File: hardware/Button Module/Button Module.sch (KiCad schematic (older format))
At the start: 10 parts, among them J1 1A, J2 1A, J3 2A, J4 2A, J5 1B, J6 1B, J7 2B, J8 2B, SW1 B3F-4055, SW2 B3F-4055

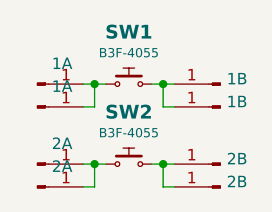
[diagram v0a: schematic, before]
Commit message: Updated instructions for RPi 4 boards
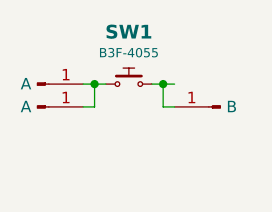
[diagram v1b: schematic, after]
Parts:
- removed J3, J4: 2A, Connector_PinHeader_2.54mm:PinHeader_1x01_P2.54mm_Vertical, symbol Connector:Conn_01x01_Male
- removed J5: 1B, Connector_PinHeader_2.54mm:PinHeader_1x01_P2.54mm_Vertical, symbol Connector:Conn_01x01_Male
- removed J7, J8: 2B, Connector_PinHeader_2.54mm:PinHeader_1x01_P2.54mm_Vertical, symbol Connector:Conn_01x01_Male
- removed SW2: B3F-4055, switches:B3F-40XX, symbol switches:MOM-SPST
- J1, J2: value 1A -> A
- J6: value 1B -> B
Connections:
- wire segments 16 -> 8
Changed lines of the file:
@@
 Comment4 ""
 $EndDescr
+Wire Wire Line
+	2750 2850 2700 2850
+Wire Wire Line
+	2800 2850 2750 2850
+Connection ~ 2750 2850
+Wire Wire Line
+	2750 2950 2750 2850
+Wire Wire Line
+	2800 2950 2750 2950
+$Comp
+L Connector:Conn_01x01_Male J6
+U 1 1 5E38EB6E
+P 3000 2950
+F 0 "J6" H 2972 2882 50  0001 R CNN
+F 1 "B" H 2950 2950 50  0000 C CNN
+F 2 "Connector_PinHeader_2.54mm:PinHeader_1x01_P2.54mm_Vertical" H 3000 2950 50  0001 C CNN
+F 3 "~" H 3000 2950 50  0001 C CNN
+	1    3000 2950
+	-1   0    0    1
+$EndComp
+$Comp
+L Connector:Conn_01x01_Male J1
+U 1 1 5E38A935
+P 2200 2850
+F 0 "J1" H 2308 3031 50  0001 C CNN
+F 1 "A" H 2150 2850 50  0000 C CNN
+F 2 "Connector_PinHeader_2.54mm:PinHeader_1x01_P2.54mm_Vertical" H 2200 2850 50  0001 C CNN
+F 3 "~" H 2200 2850 50  0001 C CNN
+	1    2200 2850
+	1    0    0    -1
+$EndComp
+Wire Wire Line
+	2400 2950 2450 2950
+$Comp
+L Connector:Conn_01x01_Male J2
+U 1 1 5E38AF59
+P 2200 2950
+F 0 "J2" H 2308 3131 50  0001 C CNN
+F 1 "A" H 2150 2950 50  0000 C CNN
+F 2 "Connector_PinHeader_2.54mm:PinHeader_1x01_P2.54mm_Vertical" H 2200 2950 50  0001 C CNN
+F 3 "~" H 2200 2950 50  0001 C CNN
+	1    2200 2950
+	1    0    0    -1
+$EndComp
+Wire Wire Line
+	2450 2850 2500 2850
+Wire Wire Line
+	2450 2950 2450 2850
+Connection ~ 2450 2850
+Wire Wire Line
+	2400 2850 2450 2850
 $Comp
 L switches:MOM-SPST SW1
@@
 	1    0    0    -1
 $EndComp
-$Comp
-L switches:MOM-SPST SW2
-U 1 1 5E389875
-P 2600 3200
-F 0 "SW2" H 2600 3427 60  0000 C CNB
-F 1 "B3F-4055" H 2600 3336 40  0000 C CNN
-F 2 "switches:B3F-40XX" H 2500 3075 40  0001 L TNN
-F 3 "" H 2525 2975 60  0001 C CNN
-F 4 "-" H 2500 3400 40  0001 L BNN "Part"
-F 5 "Switch" H 2500 3500 40  0001 L BNN "Family"
-	1    2600 3200
-	1    0    0    -1
-$EndComp
-$Comp
-L Connector:Conn_01x01_Male J1
-U 1 1 5E38A935
-P 2200 2850
-F 0 "J1" H 2308 3031 50  0001 C CNN
-F 1 "1A" H 2308 2939 50  0000 C CNN
-F 2 "Connector_PinHeader_2.54mm:PinHeader_1x01_P2.54mm_Vertical" H 2200 2850 50  0001 C CNN
-F 3 "~" H 2200 2850 50  0001 C CNN
-	1    2200 2850
-	1    0    0    -1
-$EndComp
-$Comp
-L Connector:Conn_01x01_Male J2
-U 1 1 5E38AF59
-P 2200 2950
-F 0 "J2" H 2308 3131 50  0001 C CNN
-F 1 "1A" H 2308 3039 50  0000 C CNN
-F 2 "Connector_PinHeader_2.54mm:PinHeader_1x01_P2.54mm_Vertical" H 2200 2950 50  0001 C CNN
-F 3 "~" H 2200 2950 50  0001 C CNN
-	1    2200 2950
-	1    0    0    -1
-$EndComp
-$Comp
-L Connector:Conn_01x01_Male J3
-U 1 1 5E38B268
-P 2200 3200
-F 0 "J3" H 2308 3381 50  0001 C CNN
-F 1 "2A" H 2308 3289 50  0000 C CNN
-F 2 "Connector_PinHeader_2.54mm:PinHeader_1x01_P2.54mm_Vertical" H 2200 3200 50  0001 C CNN
-F 3 "~" H 2200 3200 50  0001 C CNN
-	1    2200 3200
-	1    0    0    -1
-$EndComp
-$Comp
-L Connector:Conn_01x01_Male J4
-U 1 1 5E38B61F
-P 2200 3300
-F 0 "J4" H 2308 3481 50  0001 C CNN
-F 1 "2A" H 2308 3389 50  0000 C CNN
-F 2 "Connector_PinHeader_2.54mm:PinHeader_1x01_P2.54mm_Vertical" H 2200 3300 50  0001 C CNN
-F 3 "~" H 2200 3300 50  0001 C CNN
-	1    2200 3300
-	1    0    0    -1
-$EndComp
-Wire Wire Line
-	2400 2850 2450 2850
-Wire Wire Line
-	2400 2950 2450 2950
-Wire Wire Line
-	2450 2950 2450 2850
-Connection ~ 2450 2850
-Wire Wire Line
-	2450 2850 2500 2850
-Wire Wire Line
-	2400 3200 2450 3200
-Wire Wire Line
-	2400 3300 2450 3300
-Wire Wire Line
-	2450 3300 2450 3200
-Connection ~ 2450 3200
-Wire Wire Line
-	2450 3200 2500 3200
-$Comp
-L Connector:Conn_01x01_Male J5
-U 1 1 5E38DF3B
-P 3000 2850
-F 0 "J5" H 2972 2782 50  0001 R CNN
-F 1 "1B" H 2972 2828 50  0000 R CNN
-F 2 "Connector_PinHeader_2.54mm:PinHeader_1x01_P2.54mm_Vertical" H 3000 2850 50  0001 C CNN
-F 3 "~" H 3000 2850 50  0001 C CNN
-	1    3000 2850
-	-1   0    0    1
-$EndComp
-$Comp
-L Connector:Conn_01x01_Male J6
-U 1 1 5E38EB6E
-P 3000 2950
-F 0 "J6" H 2972 2882 50  0001 R CNN
-F 1 "1B" H 2972 2928 50  0000 R CNN
-F 2 "Connector_PinHeader_2.54mm:PinHeader_1x01_P2.54mm_Vertical" H 3000 2950 50  0001 C CNN
-F 3 "~" H 3000 2950 50  0001 C CNN
-	1    3000 2950
-	-1   0    0    1
-$EndComp
-$Comp
-L Connector:Conn_01x01_Male J7
-U 1 1 5E38F265
-P 3000 3200
-F 0 "J7" H 2972 3132 50  0001 R CNN
-F 1 "2B" H 2972 3178 50  0000 R CNN
-F 2 "Connector_PinHeader_2.54mm:PinHeader_1x01_P2.54mm_Vertical" H 3000 3200 50  0001 C CNN
-F 3 "~" H 3000 3200 50  0001 C CNN
-	1    3000 3200
-	-1   0    0    1
-$EndComp
-$Comp
-L Connector:Conn_01x01_Male J8
-U 1 1 5E38F7C0
-P 3000 3300
-F 0 "J8" H 2972 3232 50  0001 R CNN
-F 1 "2B" H 2972 3278 50  0000 R CNN
-F 2 "Connector_PinHeader_2.54mm:PinHeader_1x01_P2.54mm_Vertical" H 3000 3300 50  0001 C CNN
-F 3 "~" H 3000 3300 50  0001 C CNN
-	1    3000 3300
-	-1   0    0    1
-$EndComp
-Wire Wire Line
-	2700 3200 2750 3200
-Wire Wire Line
-	2800 2850 2750 2850
-Wire Wire Line
-	2800 2950 2750 2950
-Wire Wire Line
-	2750 2950 2750 2850
-Connection ~ 2750 2850
-Wire Wire Line
-	2750 2850 2700 2850
-Wire Wire Line
-	2800 3300 2750 3300
-Wire Wire Line
-	2750 3300 2750 3200
-Connection ~ 2750 3200
-Wire Wire Line
-	2750 3200 2800 3200
 $EndSCHEMATC
